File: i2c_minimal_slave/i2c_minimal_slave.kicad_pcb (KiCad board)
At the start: 2 copper layers, 16 x 24 mm, 13 parts, among them U1 P82B715

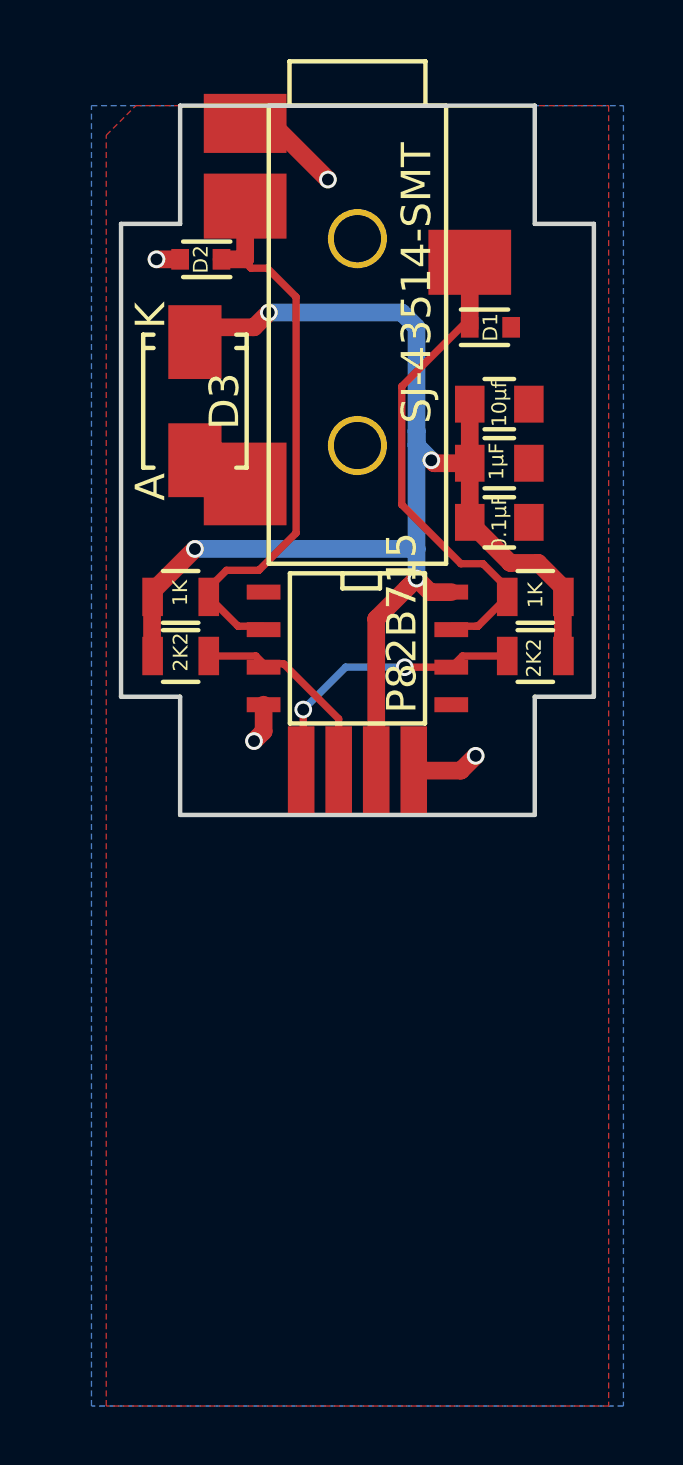
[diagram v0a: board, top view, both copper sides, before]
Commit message: more spacious slave design, matching the main-power board outline
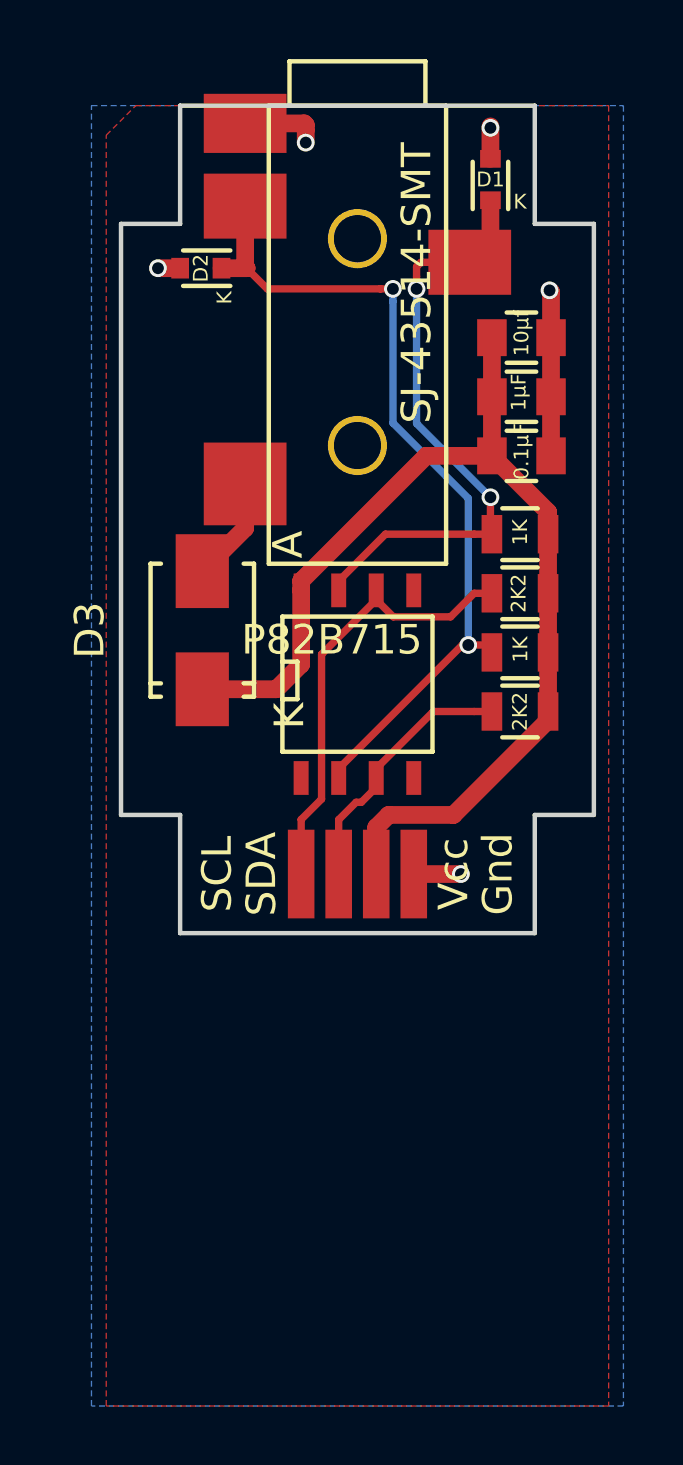
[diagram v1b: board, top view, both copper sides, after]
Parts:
- moved R2 11.6 mm to (55.5, 63.5), turned to 0 degrees
- moved R4 11.6 mm to (55.5, 65.5), turned to 0 degrees
- moved D3 7.75 mm to (44.8, 62.7), turned to 90 degrees
- moved D1 5.00 mm to (54.5, 47.5), turned to 90 degrees
- moved I2C1 3.50 mm to (50.0, 71.0)
- moved C1 2.37 mm to (55.5, 52.9)
- moved C2 2.37 mm to (55.5, 54.9)
- moved C3 2.37 mm to (55.5, 56.9)
- moved R1 2.18 mm to (55.5, 59.5)
- moved R3 2.18 mm to (55.5, 61.5)
- moved U1 1.21 mm to (50.0, 64.6), turned to 0 degrees
- moved D2 0.30 mm to (44.7, 50.5)
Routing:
- net +5V: track 49.7 -> 37.4 mm, vias 4 -> 0
- net /I2C_bridge/SDA_connector: track 19.2 -> 28.7 mm, vias 0 -> 2
- net /I2C_bridge/SCL_inside: track 9.75 -> 15.1 mm, vias 2 -> 0
- net GND: track 8.05 -> 11.7 mm, vias 4 -> 5
- net /I2C_bridge/SCL_connector: track 16.8 -> 20.2 mm, vias 0 -> 2
- net /I2C_bridge/SDA_inside: track 7.03 -> 8.91 mm
- net Net-(D3-Pad2): track 2.03 -> 3.55 mm
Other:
- board size 16 x 24 mm -> 16 x 28 mm
- board text added: "K"

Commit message: more fixes :-s
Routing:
- net GND: track 11.7 -> 16.7 mm, vias 5 -> 6
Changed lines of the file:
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@@
   (general
     (links 27)
-    (no_connects 1)
+    (no_connects 0)
     (area 33.899999 38.3 69.35 89.000001)
     (thickness 1.6)
     (drawings 40)
-    (tracks 89)
+    (tracks 94)
     (zones 0)
     (modules 13)
@@
   )
   (setup
-    (last_trace_width 0.25)
+    (last_trace_width 0.6)
     (user_trace_width 0.6)
     (trace_clearance 0.2)
@@
   (segment (start 54.55 54.85) (end 54.55 56.85) (width 0.6) (layer F.Cu) (net 1))
   (segment (start 54.55 52.85) (end 54.55 54.85) (width 0.6) (layer F.Cu) (net 1))
+  (segment (start 53.1 67.5) (end 53.1 70.6) (width 0.6) (layer B.Cu) (net 2))
+  (segment (start 53.1 70.6) (end 53.5 71) (width 0.6) (layer B.Cu) (net 2))
+  (segment (start 51.905 67.75) (end 52.85 67.75) (width 0.6) (layer F.Cu) (net 2))
+  (segment (start 52.85 67.75) (end 53.1 67.5) (width 0.6) (layer F.Cu) (net 2))
+  (via (at 53.1 67.5) (size 0.6) (drill 0.4) (layers F.Cu B.Cu) (net 2))
   (segment (start 56.55 54.85) (end 56.55 52.85) (width 0.6) (layer F.Cu) (net 2))
   (segment (start 56.55 56.85) (end 56.55 54.85) (width 0.6) (layer F.Cu) (net 2))
